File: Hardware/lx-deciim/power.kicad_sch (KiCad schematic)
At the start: 12 parts, among them IC1 AZ1117CH2-5.0TRG1, J17 Conn_01x10

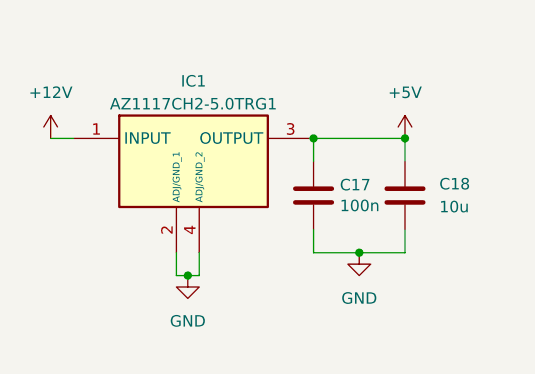
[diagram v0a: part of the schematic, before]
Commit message: feature: prep files for export (fill bom, gerber)
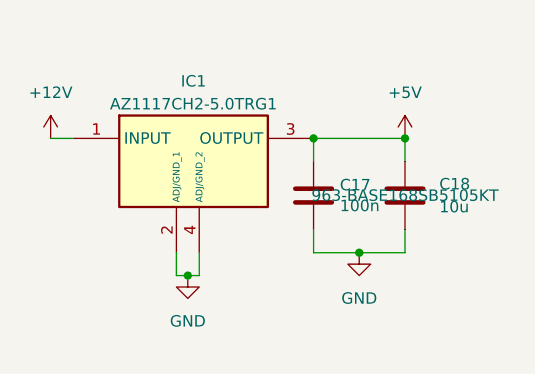
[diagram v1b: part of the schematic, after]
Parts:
- C15, C19: Mouser Part Number 581-06031C104MAT2A -> 710-885012206071R
- C18: Mouser Part Number (none) -> 963-BASE168SB5105KT
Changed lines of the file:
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@@
 			)
 		)
-		(property "Mouser Part Number" "581-06031C104MAT2A"
+		(property "Mouser Part Number" "710-885012206071R"
 			(at 125.73 99.06 0)
 			(effects
@@
 			)
 		)
+		(property "Mouser Part Number" "963-BASE168SB5105KT"
+			(at 198.12 93.98 0)
+			(effects
+				(font
+					(size 1.27 1.27)
+				)
+			)
+		)
 		(pin "1"
 		)
@@
 			)
 		)
-		(property "Mouser Part Number" "581-06031C104MAT2A"
+		(property "Mouser Part Number" "710-885012206071R"
 			(at 125.73 88.9 0)
 			(effects

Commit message: fix: fix mouser part number on schematic + fill page settings
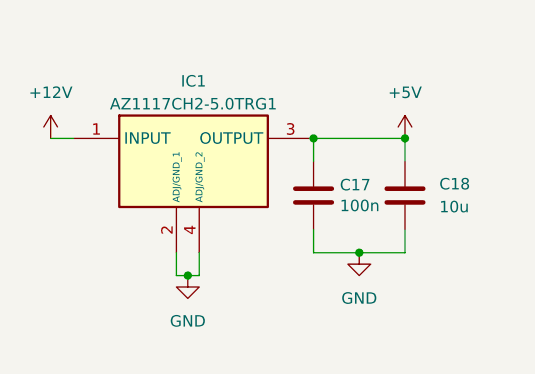
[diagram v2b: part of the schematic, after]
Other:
- company: (none) -> Lucas Bonvin
- title: (none) -> lx-deciim
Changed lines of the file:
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@@
 	(generator_version "9.0")
 	(paper "A4")
+	(title_block
+		(title "lx-deciim")
+		(date "2025-06-17")
+		(rev "v1.0.0")
+		(company "Lucas Bonvin")
+		(comment 1 "This project is licensed under the CC BY-NC 4.0 License.")
+	)
 	(junction
 		(at 135.89 104.14)
@@
 					(size 1.27 1.27)
 				)
-			)
-		)
+				(hide yes)
+			)
+		)
